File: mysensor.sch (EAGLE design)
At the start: 35 parts, among them IC1 LD117AS12TR, IC3 MEGA8-AI

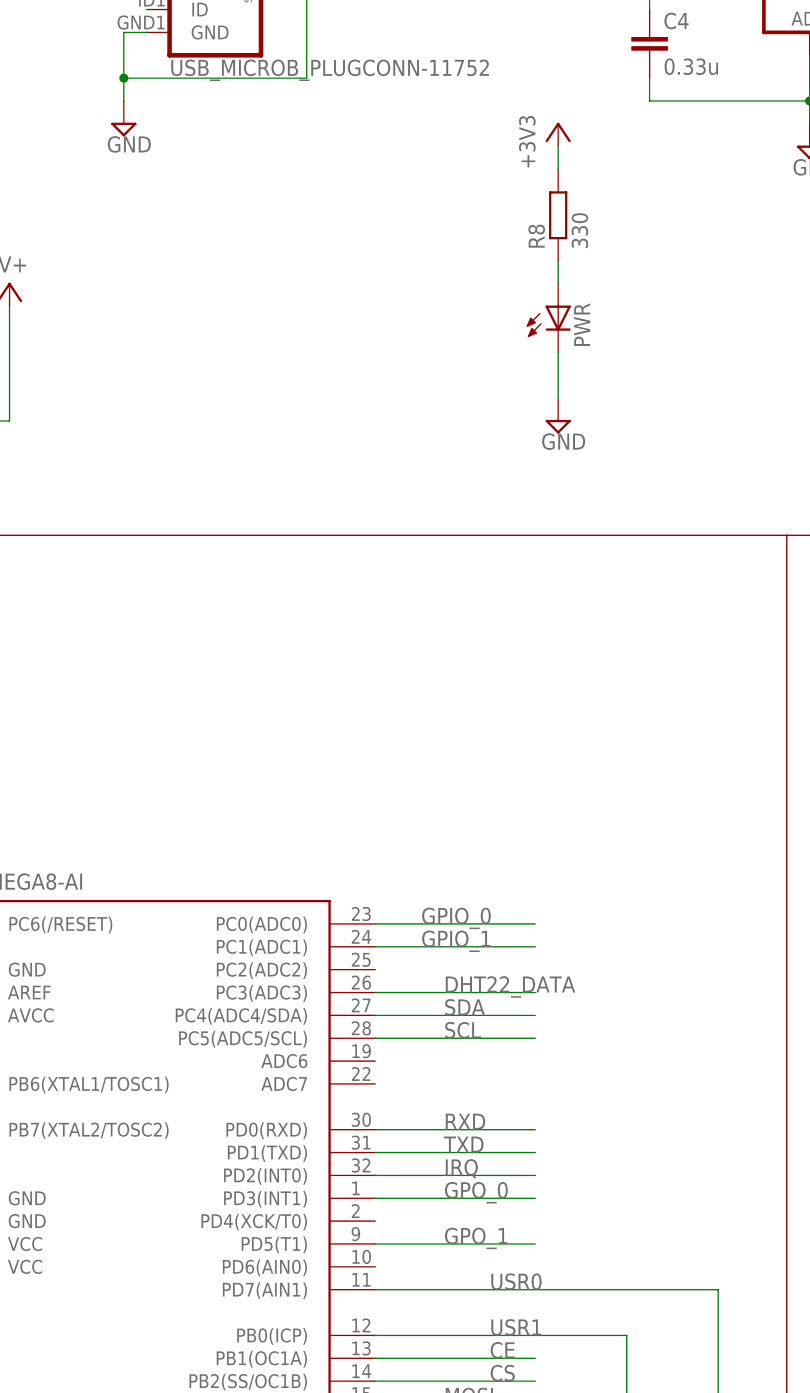
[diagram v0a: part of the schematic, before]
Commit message: Updates  for rev 1.0
* Moved LDO to left, too close to pin header
* Moved USR1/2 to right for not covered by wifi module
* Removed ground plane under pcb antenna
* Moved GPIO_1 to INT1
* Possible to read battery power by ADC
* Add V+ and GND text to skruvplint

Signed-off-by: Marcus Folkesson <marcus.folkesson@gmail.com>
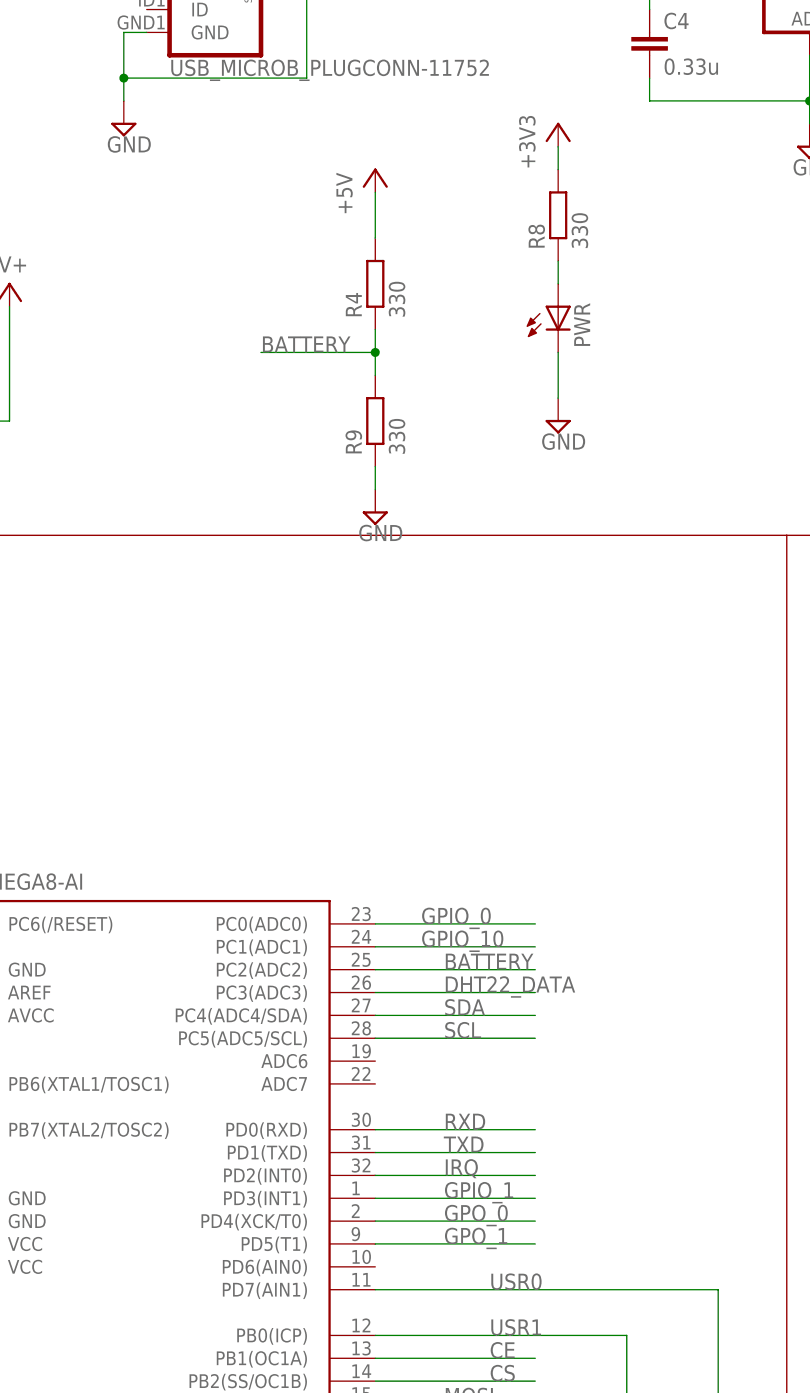
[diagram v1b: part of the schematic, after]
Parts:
- added R4, R9: 330, rcl:R-EU_M0805
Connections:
- new net BATTERY: IC3.PC2(ADC2), R4.1, R9.2
- new net GPIO_10: IC3.PC1(ADC1)
- net +5V: now also R4.2
- net GND: now also R9.1
- net GPIO_1: now also IC3.PD3(INT1); no longer IC3.PC1(ADC1)
- net GPO_0: now also IC3.PD4(XCK/T0); no longer IC3.PD3(INT1)
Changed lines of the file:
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@@
 <part name="SUPPLY13" library="supply2" deviceset="GND" device=""/>
 <part name="R3" library="rcl" deviceset="R-EU_" device="M0805" value="330"/>
+<part name="P+3" library="supply1" deviceset="+5V" device=""/>
+<part name="R4" library="rcl" deviceset="R-EU_" device="M0805" value="330"/>
+<part name="R9" library="rcl" deviceset="R-EU_" device="M0805" value="330"/>
+<part name="SUPPLY19" library="supply2" deviceset="GND" device=""/>
 </parts>
 <sheets>
@@
 <instance part="SUPPLY13" gate="GND" x="50.8" y="-83.82"/>
 <instance part="R3" gate="G$1" x="50.8" y="-60.96" rot="R90"/>
+<instance part="P+3" gate="1" x="22.86" y="86.36"/>
+<instance part="R4" gate="G$1" x="22.86" y="73.66" rot="R90"/>
+<instance part="R9" gate="G$1" x="22.86" y="58.42" rot="R90"/>
+<instance part="SUPPLY19" gate="GND" x="22.86" y="48.26"/>
 </instances>
 <busses>
@@
 <pinref part="P+4" gate="1" pin="+5V"/>
 <pinref part="GPO1" gate="G$1" pin="2"/>
+</segment>
+<segment>
+<pinref part="R4" gate="G$1" pin="2"/>
+<pinref part="P+3" gate="1" pin="+5V"/>
+<wire x1="22.86" y1="78.74" x2="22.86" y2="83.82" width="0.1524" layer="91"/>
 </segment>
 </net>
@@
 <wire x1="50.8" y1="-81.28" x2="50.8" y2="-76.2" width="0.1524" layer="91"/>
 </segment>
+<segment>
+<pinref part="SUPPLY19" gate="GND" pin="GND"/>
+<pinref part="R9" gate="G$1" pin="1"/>
+<wire x1="22.86" y1="50.8" x2="22.86" y2="53.34" width="0.1524" layer="91"/>
+</segment>
 </net>
 <net name="TXD" class="0">
@@
 <net name="GPIO_1" class="0">
 <segment>
-<wire x1="22.86" y1="0" x2="40.64" y2="0" width="0.1524" layer="91"/>
-<label x="27.94" y="0" size="1.778" layer="95"/>
-<pinref part="IC3" gate="G$1" pin="PC1(ADC1)"/>
-</segment>
-<segment>
 <pinref part="R5" gate="G$1" pin="1"/>
 <wire x1="129.54" y1="78.74" x2="119.38" y2="78.74" width="0.1524" layer="91"/>
 <label x="119.38" y="78.74" size="1.778" layer="95"/>
+</segment>
+<segment>
+<wire x1="22.86" y1="-27.94" x2="40.64" y2="-27.94" width="0.1524" layer="91"/>
+<label x="30.48" y="-27.94" size="1.778" layer="95"/>
+<pinref part="IC3" gate="G$1" pin="PD3(INT1)"/>
 </segment>
 </net>
@@
 </segment>
 <segment>
-<wire x1="22.86" y1="-27.94" x2="40.64" y2="-27.94" width="0.1524" layer="91"/>
-<label x="30.48" y="-27.94" size="1.778" layer="95"/>
-<pinref part="IC3" gate="G$1" pin="PD3(INT1)"/>
+<pinref part="IC3" gate="G$1" pin="PD4(XCK/T0)"/>
+<wire x1="22.86" y1="-30.48" x2="40.64" y2="-30.48" width="0.1524" layer="91"/>
+<label x="30.48" y="-30.48" size="1.778" layer="95"/>
 </segment>
 </net>
@@
 </segment>
 </net>
+<net name="GPIO_10" class="0">
+<segment>
+<wire x1="22.86" y1="0" x2="40.64" y2="0" width="0.1524" layer="91"/>
+<label x="27.94" y="0" size="1.778" layer="95"/>
+<pinref part="IC3" gate="G$1" pin="PC1(ADC1)"/>
+</segment>
+</net>
+<net name="BATTERY" class="0">
+<segment>
+<pinref part="IC3" gate="G$1" pin="PC2(ADC2)"/>
+<wire x1="22.86" y1="-2.54" x2="40.64" y2="-2.54" width="0.1524" layer="91"/>
+<label x="30.48" y="-2.54" size="1.778" layer="95"/>
+</segment>
+<segment>
+<pinref part="R9" gate="G$1" pin="2"/>
+<pinref part="R4" gate="G$1" pin="1"/>
+<wire x1="22.86" y1="63.5" x2="22.86" y2="66.04" width="0.1524" layer="91"/>
+<wire x1="22.86" y1="66.04" x2="22.86" y2="68.58" width="0.1524" layer="91"/>
+<wire x1="22.86" y1="66.04" x2="10.16" y2="66.04" width="0.1524" layer="91"/>
+<junction x="22.86" y="66.04"/>
+<label x="10.16" y="66.04" size="1.778" layer="95"/>
+</segment>
+</net>

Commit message: Unknown changes
Signed-off-by: Marcus Folkesson <marcus.folkesson@gmail.com>
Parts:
- added R11: 4.7k, rcl:R-EU_M0805
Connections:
- new net N$7: R11.1, U$1.P$3, U$1.P$4
- new net NO: IC3.PD4(XCK/T0)
- net +3V3: now also R11.2
- net GPO_0: now also IC3.PD5(T1); no longer IC3.PD4(XCK/T0)
- net GPO_1: now also IC3.PD6(AIN0); no longer IC3.PD5(T1)
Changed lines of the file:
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@@
 <part name="R9" library="rcl" deviceset="R-EU_" device="M0805" value="330"/>
 <part name="SUPPLY19" library="supply2" deviceset="GND" device=""/>
+<part name="R11" library="rcl" deviceset="R-EU_" device="M0805" value="4.7k"/>
 </parts>
 <sheets>
@@
 <instance part="R9" gate="G$1" x="22.86" y="58.42" rot="R90"/>
 <instance part="SUPPLY19" gate="GND" x="22.86" y="48.26"/>
+<instance part="R11" gate="G$1" x="142.24" y="12.7" rot="R90"/>
 </instances>
 <busses>
@@
 <wire x1="127" y1="-5.08" x2="134.62" y2="-5.08" width="0.1524" layer="91"/>
 <pinref part="+3V2" gate="G$1" pin="+3V3"/>
-<wire x1="134.62" y1="-5.08" x2="134.62" y2="25.4" width="0.1524" layer="91"/>
+<wire x1="134.62" y1="-5.08" x2="134.62" y2="20.32" width="0.1524" layer="91"/>
+<pinref part="R11" gate="G$1" pin="2"/>
+<wire x1="134.62" y1="20.32" x2="134.62" y2="25.4" width="0.1524" layer="91"/>
+<wire x1="142.24" y1="17.78" x2="142.24" y2="20.32" width="0.1524" layer="91"/>
+<wire x1="142.24" y1="20.32" x2="134.62" y2="20.32" width="0.1524" layer="91"/>
+<junction x="134.62" y="20.32"/>
 </segment>
 <segment>
@@
 </segment>
 <segment>
-<pinref part="IC3" gate="G$1" pin="PD4(XCK/T0)"/>
-<wire x1="22.86" y1="-30.48" x2="40.64" y2="-30.48" width="0.1524" layer="91"/>
-<label x="30.48" y="-30.48" size="1.778" layer="95"/>
+<pinref part="IC3" gate="G$1" pin="PD5(T1)"/>
+<wire x1="22.86" y1="-33.02" x2="40.64" y2="-33.02" width="0.1524" layer="91"/>
+<label x="30.48" y="-33.02" size="1.778" layer="95"/>
 </segment>
 </net>
@@
 </segment>
 <segment>
-<pinref part="IC3" gate="G$1" pin="PD5(T1)"/>
-<wire x1="22.86" y1="-33.02" x2="40.64" y2="-33.02" width="0.1524" layer="91"/>
-<label x="30.48" y="-33.02" size="1.778" layer="95"/>
+<pinref part="IC3" gate="G$1" pin="PD6(AIN0)"/>
+<wire x1="22.86" y1="-35.56" x2="40.64" y2="-35.56" width="0.1524" layer="91"/>
+<label x="30.48" y="-35.56" size="1.778" layer="95"/>
 </segment>
 </net>
@@
 </segment>
 </net>
+<net name="NO" class="0">
+<segment>
+<pinref part="IC3" gate="G$1" pin="PD4(XCK/T0)"/>
+<wire x1="22.86" y1="-30.48" x2="40.64" y2="-30.48" width="0.1524" layer="91"/>
+<label x="30.48" y="-30.48" size="1.778" layer="95"/>
+</segment>
+</net>
+<net name="N$7" class="0">
+<segment>
+<pinref part="U$1" gate="G$1" pin="P$3"/>
+<pinref part="R11" gate="G$1" pin="1"/>
+<wire x1="127" y1="-2.54" x2="142.24" y2="-2.54" width="0.1524" layer="91"/>
+<wire x1="142.24" y1="-2.54" x2="142.24" y2="0" width="0.1524" layer="91"/>
+<pinref part="U$1" gate="G$1" pin="P$4"/>
+<wire x1="142.24" y1="0" x2="142.24" y2="7.62" width="0.1524" layer="91"/>
+<wire x1="127" y1="0" x2="142.24" y2="0" width="0.1524" layer="91"/>
+<junction x="142.24" y="0"/>
+</segment>
+</net>
